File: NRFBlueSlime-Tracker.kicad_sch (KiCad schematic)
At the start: 70 parts, among them J1 GT-USB-7010ASV, SW1 TS-1088-AR02016, U1 nRF52840, U2 EA8103DHR, U3 BQ24075RGT, U4 ICM-45686, U5 LIS2MDL, X1 S2D32.768KB20F30T, Y1 XKXGI-SUA-32.768K, Y2 XL7EL89CKI-111YLC-32M

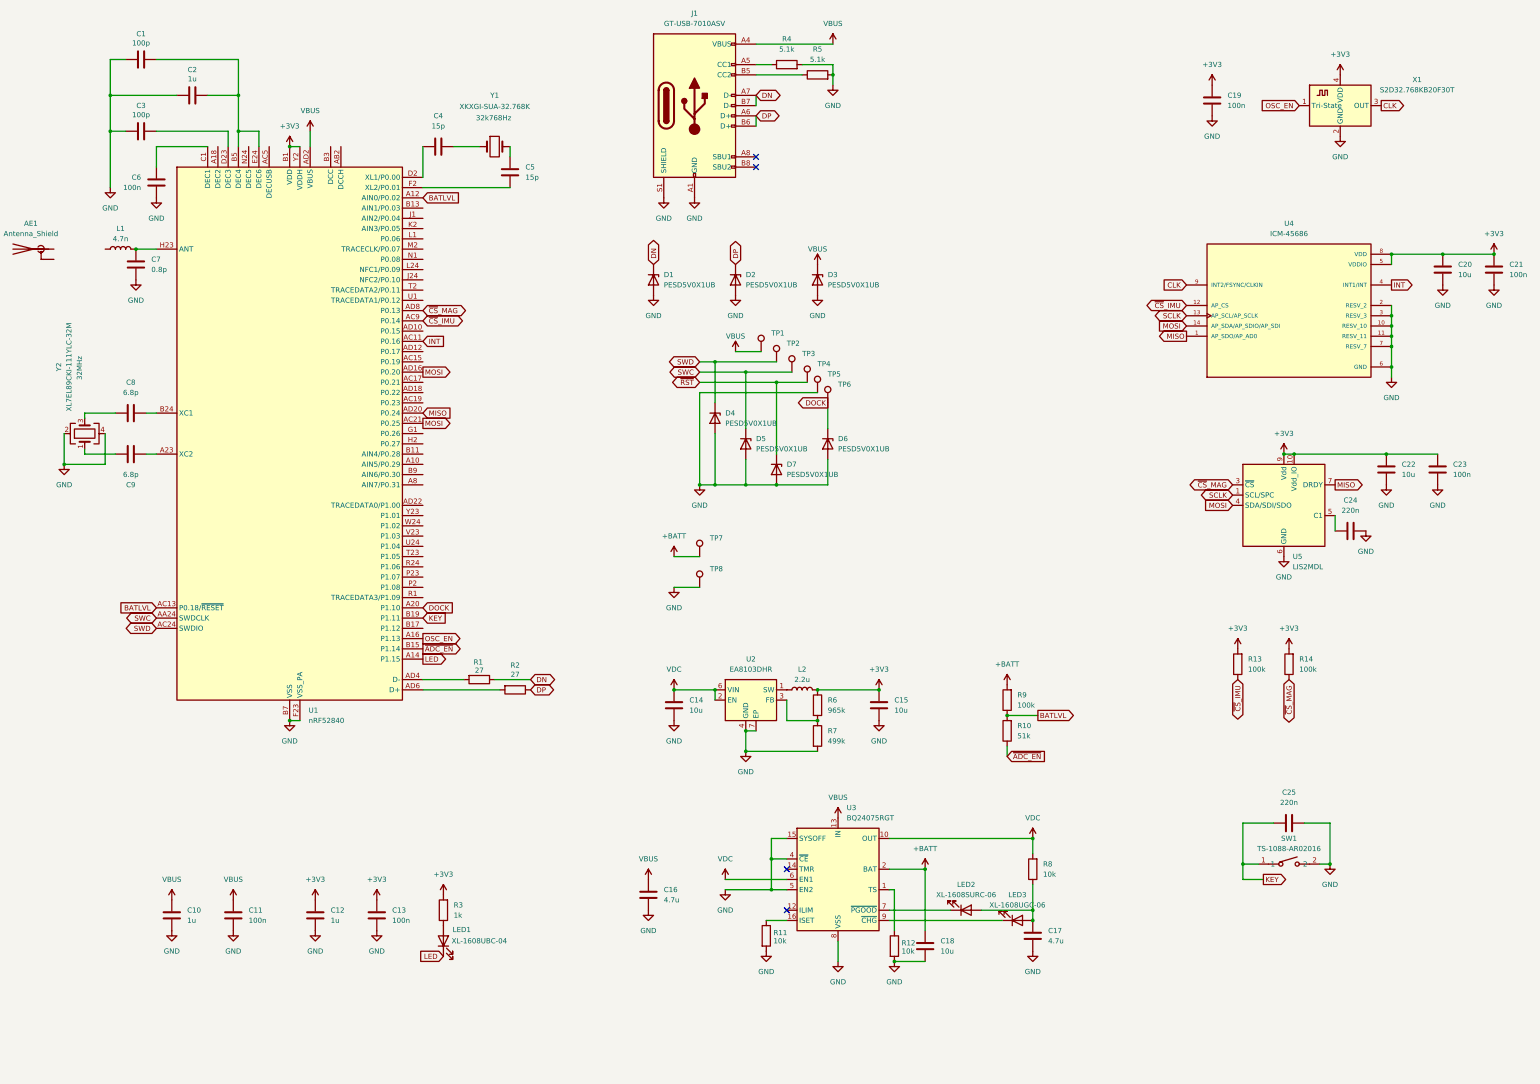
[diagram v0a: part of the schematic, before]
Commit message: rework LEDs
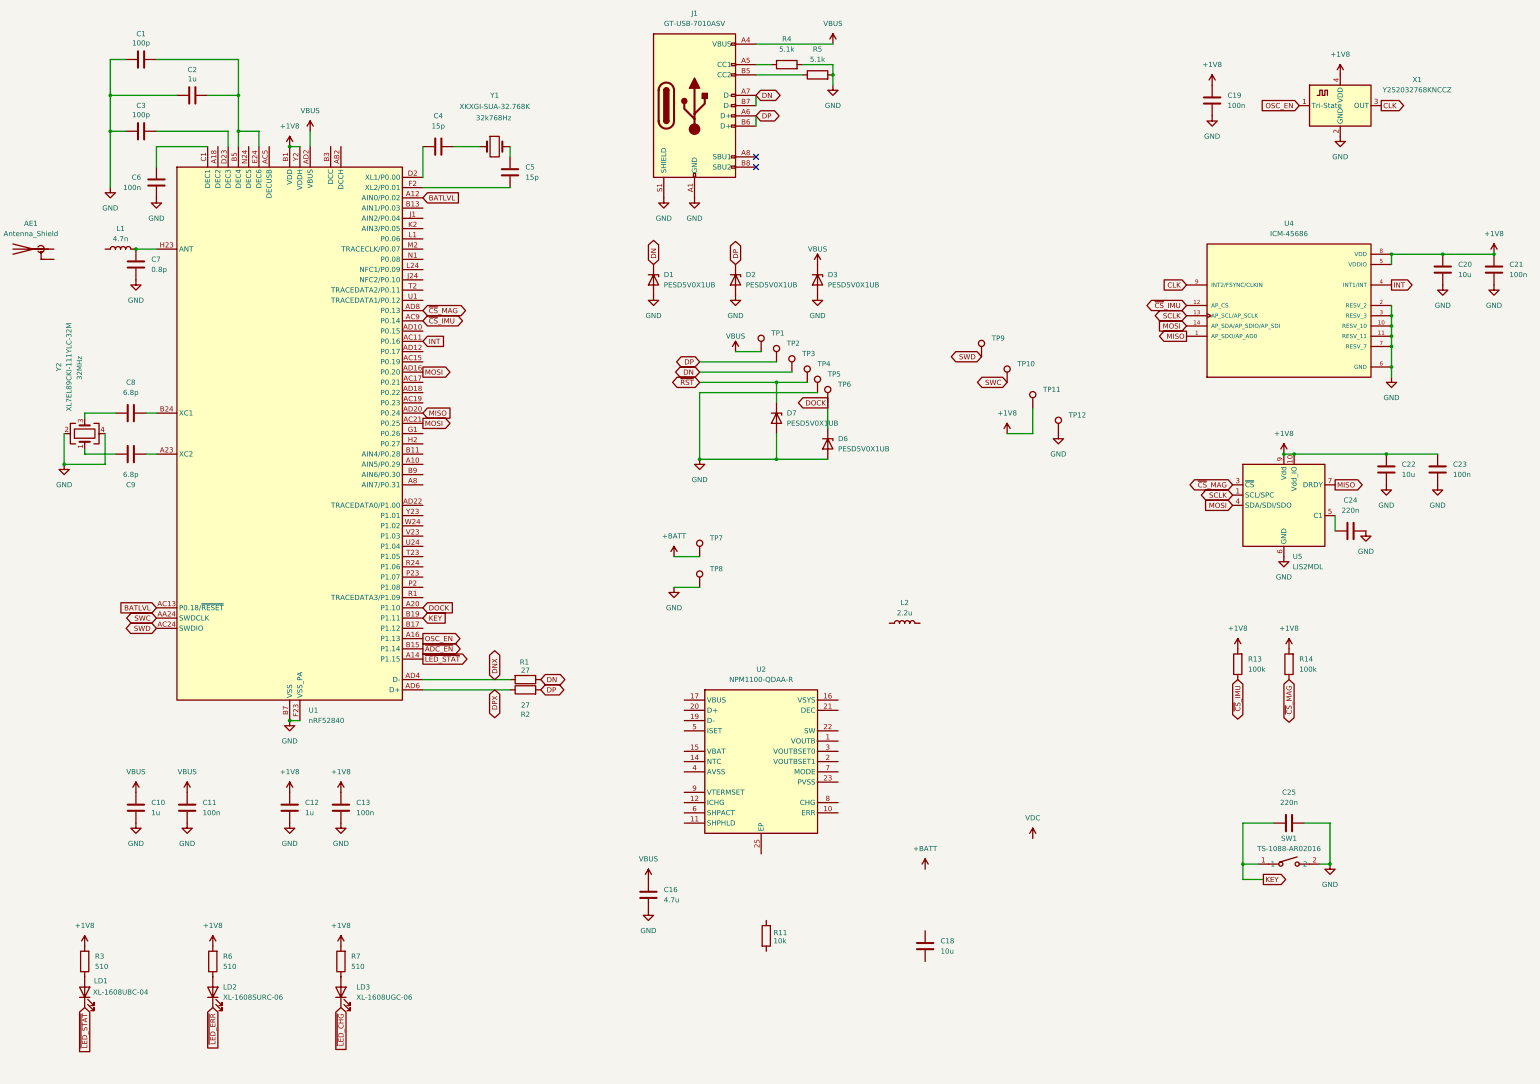
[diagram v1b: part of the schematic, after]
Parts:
- removed C14, C15: 10u, Capacitor_SMD:C_0603_1608Metric, symbol Device:C
- removed C17: 4.7u, Capacitor_SMD:C_0603_1608Metric, symbol Device:C
- removed D4, D5: PESD5V0X1UB, Diode_SMD:D_SOD-882, symbol Diode:PESD5V0L1UL
- removed R10: 51k, Resistor_SMD:R_0603_1608Metric, symbol Device:R
- removed R12, R8: 10k, Resistor_SMD:R_0402_1005Metric, symbol Device:R
- removed R9: 100k, Resistor_SMD:R_0603_1608Metric, symbol Device:R
- removed U2: EA8103DHR, nrfslime:DFN-6_L1.5-W1.5-P0.50-BL-EP1.0, symbol nrfslime:EA8103DHR
- removed U3: BQ24075RGT, Package_DFN_QFN:VQFN-16-1EP_3x3mm_P0.5mm_EP1.6x1.6mm, symbol Battery_Management:BQ24075RGT
- added TP10, TP11, TP12, TP9: TestPoint, TestPoint:TestPoint_Pad_1.0x1.0mm, symbol Connector:TestPoint
- added U2: NPM1100-QDAA-R, npm1100-q:QFN50P400X400X90-25N-D, symbol NPM1100-QDAA-R:NPM1100-QDAA-R
- R3: value 1k -> 510
- R6: value 965k -> 510
- R7: value 499k -> 510
- X1: value S2D32.768KB20F30T -> Y252032768KNCCZ
- renumbered LED1 to LD1, LED2 to LD2, LED3 to LD3
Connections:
- net +BATT: no longer C18.2
- net DN: now also TP3.1
- net DP: now also R2.2, TP2.1; no longer R2.1
- net GND: now also TP12.1; no longer C18.1, R11.2, R7.2
- net SWC: now also TP10.1; no longer TP3.1
- net SWD: now also TP9.1; no longer TP2.1
- net at LD3.2 (A): now also R7.1; no longer LD2.2 (A)
- net DNX: now reaches R1.2, U1.AD4 (D-)
- net +1V8: now reaches R6.2
- net +1V8: now also C12.1, C13.1, C19.1, C20.1, C21.1, C22.1, C23.1, R13.2, R14.2, R3.2, R7.2, U1.A22 (VDD), U1.AD14 (VDD), U1.AD23 (VDD), U1.B1 (VDD), U1.W1 (VDD), U1.Y2 (VDDH), U4.5 (VDDIO), U4.8 (VDD), U5.10 (Vdd_IO), U5.9 (Vdd), X1.4 (VDD), TP11.1; no longer R7.1
- net ~{LED_CHG}: now reaches LD3.1 (K)
- net ~{LED_ERR}: now reaches LD2.1 (K)
- net DPX: now reaches U1.AD6 (D+)
- net DPX: now also R2.1; no longer R2.2
- removed net +3V3: C12.1, C13.1, C19.1, C20.1, C21.1, C22.1, C23.1, L2.2, R13.2, R14.2, R3.2, R6.1, U1.A22 (VDD), U1.AD14 (VDD), U1.AD23 (VDD), U1.B1 (VDD), U1.W1 (VDD), U1.Y2 (VDDH), U4.5 (VDDIO), U4.8 (VDD), U5.10 (Vdd_IO), U5.9 (Vdd), X1.4 (VDD)
- net LED renamed ~{LED_STAT}
- new net: LD2.2 (A), R6.1
- no-connect marks 4 -> 2
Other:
- moved on the sheet: C10, C11, C12, C13, D7, L2, LD1, LD2, LD3, R1, R2, R3

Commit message: complete nPM
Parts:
- added C14, C15: 10u, Capacitor_SMD:C_0603_1608Metric, symbol Device:C
- added C17: 1u, Capacitor_SMD:C_0603_1608Metric, symbol Device:C
- added R10, R8, R9: 100k, Resistor_SMD:R_0402_1005Metric, symbol Device:R
- added TH1: HNTC0402-103F3380FB, Resistor_SMD:R_0402_1005Metric, symbol Device:Thermistor_NTC
- added TP13, TP14: TestPoint, TestPoint:TestPoint_Pad_1.0x1.0mm, symbol Connector:TestPoint
- C16: value 4.7u -> 2.2u
- R11: value 10k -> 4.7k
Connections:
- net +1V8: now also L2.2, U2.1 (VOUTB), C15.1
- net +BATT: now also U2.15 (VBAT), C17.2, R9.1
- net DN: now also R1.2, U1.AD4 (D-), U2.19 (D-); no longer J1.A7 (D-), J1.B7 (D-), R1.1
- net DNX: now also J1.A7 (D-), J1.B7 (D-), R1.1; no longer R1.2, U1.AD4 (D-)
- net DP: now also R2.1, U1.AD6 (D+), U2.20 (D+); no longer J1.A6 (D+), J1.B6 (D+), R2.2
- net DPX: now also J1.A6 (D+), J1.B6 (D+), R2.2; no longer R2.1, U1.AD6 (D+)
- net GND: now also C18.1, R11.2, U2.2 (VOUTBSET1), U2.23 (PVSS), U2.25 (EP), U2.4 (AVSS), C14.1, C15.2, C17.1, R10.1, R8.1, TH1.2
- net VBUS: now also U2.17 (VBUS)
- net ~{LED_CHG}: now also U1.L1 (P0.06)
- net ~{LED_ERR}: now also U1.N1 (P0.08)
- net at L2.1: now also U2.22 (SW)
- net VSYS: now reaches C18.2
- net VSYS: now also U2.16 (VSYS), U2.3 (VOUTBSET0), U2.9 (VTERMSET)
- net ISET: now reaches U1.R24 (P1.06)
- net ISET: now also U2.5 (ISET), R10.2
- net MODE: now reaches U1.T23 (P1.05)
- net MODE: now also U2.7 (MODE), R8.2
- net ~{NPM_ERR}: now reaches U1.U24 (P1.04)
- net ~{NPM_ERR}: now also U2.10 (ERR)
- net ~{NPM_CHG}: now reaches U1.V23 (P1.03)
- net ~{NPM_CHG}: now also U2.8 (CHG)
- net at R11.1: now also U2.12 (ICHG)
- net at U2.11 (SHPHLD): now also R9.2
- net NTC: now reaches U2.14 (NTC)
- net NTC: now also TH1.1, TP13.1
- net at U2.21 (DEC): now also C14.2
- net SHPACT: now reaches U2.6 (SHPACT)
- net SHPACT: now also TP14.1
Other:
- moved on the sheet: C16, C18, L2, R11, TP10, TP11, TP12, U2

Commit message: do usb dual mode
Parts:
- added C1: 4.7u, Capacitor_SMD:C_0603_1608Metric, symbol Device:C
- added L1: MGFL2012F150MT-LF, Inductor_SMD:L_0805_2012Metric, symbol Device:L
- added L2, L3: MLZ2012N100LT000, Inductor_SMD:L_0805_2012Metric, symbol Device:L
- added R1, R2: 0, Resistor_SMD:R_0603_1608Metric, symbol Device:R
- added R5: 1, Resistor_SMD:R_0603_1608Metric, symbol Device:R
- C11: renamed from C10; value 1u -> 4.7u
- C13: renamed from C12; value 1u -> 4.7u
- renumbered C9 to C10, C11 to C12, C13 to C14, C14 to C15, C18 to C16, C15 to C17, C16 to C18, C17 to C19, C1 to C2, C19 to C20, C20 to C21, C21 to C22, C22 to C23, C23 to C24, C24 to C25, C25 to C26, C2 to C3, C3 to C4, C4 to C5, C5 to C6, C6 to C7, C7 to C8, C8 to C9, D7 to D4, D6 to D5, L1 to L4, L2 to L5, R5 to R10, R9 to R11, R11 to R12, R8 to R13, R10 to R14, R13 to R15, R14 to R16, R1 to R3, R2 to R4, R3 to R6, R6 to R7, R7 to R8, R4 to R9, TP11 to TP10, TP12 to TP11, TP7 to TP12, TP8 to TP14, TP9 to TP7, TP14 to TP8, TP10 to TP9, U4 to U3, U5 to U4
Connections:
- net +1V8: now also L2.1, R1.2; no longer U1.Y2 (VDDH)
- net GND: now also C10.1, C9.1, C1.1
- net MOSI: no longer U1.AC21 (P0.25)
- net VBUS: now also R5.1; no longer C11.1, C12.1, U1.AD2 (VBUS)
- net ~{RST}: now also U1.AC13 (P0.18/~{RESET})
- net at Y2.3: now also C9.2, U1.B24 (XC1); no longer C9.1
- net at Y2.1: now also C10.2, U1.A23 (XC2); no longer C10.1
- net at C2.2, C3.2, U1.B5 (DEC4)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: now also L1.1
- net at U1.AB2 (DCCH): now also L2.2
- net at U1.AC5 (DECUSB): now also C1.2
- net at U1.B3 (DCC): now also L3.2
- net BATLVL: no longer names the net of U1.A12 (AIN0/P0.02)
- net BATLVL: no longer U1.AC13 (P0.18/~{RESET})
- net ISET renamed NPM_ISET
- net MODE renamed NPM_MODE
- net ~{NPM_CHG} renamed NPM_~{CHG}
- net ~{NPM_ERR} renamed NPM_~{ERR}
- new net: R1.1, R2.2, U1.Y2 (VDDH)
- new net: L1.2, L3.1
- new net VBUS_NRF: C11.1, C12.1, R2.1, R5.2, U1.AD2 (VBUS)
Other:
- moved on the sheet: AE1, C10, C11, C12, C13, C14, C2, C20, C21, C22, C23, C24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

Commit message: done sch
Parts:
- removed C5: 15p, Capacitor_SMD:C_0402_1005Metric, symbol Device:C
- removed L2, L3: MLZ2012N100LT000, Inductor_SMD:L_0805_2012Metric, symbol Device:L
- removed Y1: XKXGI-SUA-32.768K, Crystal:Crystal_SMD_3215-2Pin_3.2x1.5mm, symbol Device:Crystal
- added C14, C20: 1n, Capacitor_SMD:C_0402_1005Metric, symbol Device:C
- added Q1: YFW2301T, Package_TO_SOT_SMD:SOT-523, symbol Transistor_FET:Q_PMOS_GSD
- added R11: 1M, Resistor_SMD:R_0402_1005Metric, symbol Device:R
- added R16: 470k, Resistor_SMD:R_0402_1005Metric, symbol Device:R
- AE1: footprint (none) -> nrfslime:MIFA_BLE_ANT
- C6: value 15p -> 1.2p
- C7: renamed from C8; value 0.8p -> 1p
- L1: value MGFL2012F150MT-LF -> 2.2n; footprint Inductor_SMD:L_0805_2012Metric -> Inductor_SMD:L_0402_1005Metric; now fitted
- R14: renamed from R13; value 100k -> 470k
- R15: renamed from R14; value 100k -> 470k
- R17: renamed from R15; value 100k -> 470k
- R18: renamed from R16; value 100k -> 470k
- X1: value Y252032768KNCCZ -> SX2M32.768KM20F30TNN
- renumbered C11 to C10, C12 to C11, C13 to C12, C14 to C13, C20 to C21, C21 to C22, C22 to C23, C23 to C24, C24 to C25, C25 to C26, C26 to C27, C7 to C5, C9 to C8, C10 to C9, L4 to L2, L5 to L3, R11 to R12, R12 to R13, TP7 to TP1, TP5 to TP10, TP12 to TP11, TP13 to TP12, TP6 to TP13, TP8 to TP2, TP9 to TP3, TP10 to TP4, TP11 to TP5, TP1 to TP6, TP2 to TP7, TP3 to TP8, TP4 to TP9, Y2 to Y1
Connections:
- net +1V8: now also Q1.3 (D); no longer C21.1, X1.4 (VDD)
- net CLK: now also U1.D2 (XL1/P0.00)
- net GND: now also AE1.2 (Shield), C6.1, U1.F2 (XL2/P0.01), C14.2, C20.2, R11.2, R16.1; no longer J1.S1 (SHIELD)
- net at C2.2, C3.2, U1.B5 (DEC4)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: no longer L1.1
- net at AE1.1 (A): now also L1.1
- net at L1.2: now also C6.2, L2.1
- net OSC_EN: no longer names the net of X1.1 (Tri-State)
- net OSC_EN: now also C21.1, X1.4 (VDD), Q1.2 (S); no longer U1.A16 (P1.13)
- new net: C14.1, J1.S1 (SHIELD), R11.1
- new net ~{OSC_EN}: C20.1, Q1.1 (G), R16.2, U1.A16 (P1.13)
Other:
- moved on the sheet: AE1, C15, C16, C17, C18, C19, C21, C22, C23, C24, C25, C26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

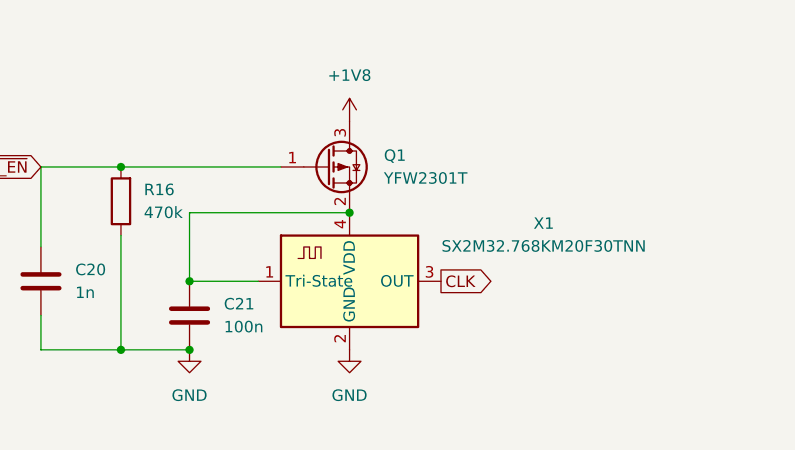
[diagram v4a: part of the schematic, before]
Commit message: fix mosfet upside down
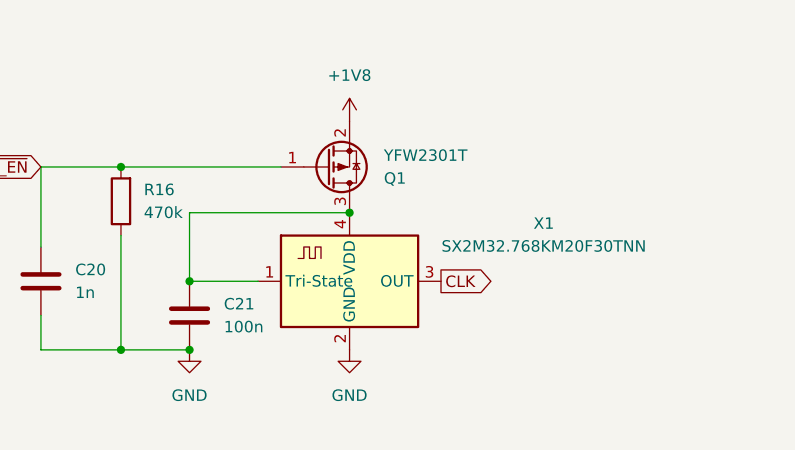
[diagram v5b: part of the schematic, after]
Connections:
- net +1V8: now also Q1.2 (S); no longer Q1.3 (D)
- net at C21.1, X1.1 (Tri-State), X1.4 (VDD): now also Q1.3 (D); no longer Q1.2 (S)
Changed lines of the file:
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@@
 	)
 	(junction
+		(at 355.6 44.45)
+		(diameter 0)
+		(color 0 0 0 0)
+	)
+	(junction
 		(at 44.45 53.34)
 		(diameter 0)
@@
 	)
 	(junction
-		(at 355.6 44.45)
-		(diameter 0)
-		(color 0 0 0 0)
-	)
-	(junction
 		(at 266.7 203.2)
 		(diameter 0)
@@
 		(lib_id "Transistor_FET:Q_PMOS_GSD")
 		(at 353.06 39.37 0)
+		(mirror x)
 		(unit 1)
 		(exclude_from_sim no)
@@
 		(on_board yes)
 		(dnp no)
-		(fields_autoplaced yes)
 		(property "Reference" "Q1"
-			(at 359.41 38.0999 0)
+			(at 359.41 40.6401 0)
 			(effects
 				(font
@@
 		)
 		(property "Value" "YFW2301T"
-			(at 359.41 40.6399 0)
+			(at 359.41 38.1001 0)
 			(effects
 				(font
@@
 		)
 		(property "Footprint" "Package_TO_SOT_SMD:SOT-523"
-			(at 358.14 36.83 0)
+			(at 358.14 41.91 0)
 			(effects
 				(font

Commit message: place components
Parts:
- C14: value 1n -> 100n
- J1: value GT-USB-7010ASV -> HC-TYPE-C-16P-C10B; footprint Connector_USB:USB_C_Receptacle_G-Switch_GT-USB-7010ASV -> nrfslime:USB-C-SMD_HC-TYPE-C-16P-C10B
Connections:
- net DN: no longer D1.1 (K)
- net DNX: now also D1.1 (K)
- net DP: no longer D2.1 (K)
- net DPX: now also D2.1 (K)
- net INT: now also U1.AD10 (P0.15); no longer U1.AC11 (P0.16)
- net NPM_MODE: now also U1.P23 (P1.07); no longer U1.T23 (P1.05)
- net NPM_~{CHG}: now also U1.W24 (P1.02); no longer U1.V23 (P1.03)
- net SCLK: now also U1.AC21 (P0.25)
- net ~{ADC_EN}: now also U1.A8 (AIN7/P0.31); no longer U1.B15 (P1.14)
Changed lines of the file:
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@@
 		)
 	)
-	(global_label "~{ADC_EN}"
-		(shape output)
-		(at 121.92 181.61 0)
-		(fields_autoplaced yes)
-		(effects
-			(font
-				(size 1.27 1.27)
-			)
-			(justify left)
-		)
-		(property "Intersheetrefs" "${INTERSHEET_REFS}"
-			(at 131.9809 181.61 0)
-			(effects
-				(font
-					(size 1.524 1.524)
-				)
-				(justify left)
-				(hide yes)
-			)
-		)
-	)
 	(global_label "MOSI"
 		(shape output)
@@
 		)
 	)
-	(global_label "NPM_~{CHG}"
-		(shape input)
-		(at 121.92 153.67 0)
-		(fields_autoplaced yes)
-		(effects
-			(font
-				(size 1.27 1.27)
-			)
-			(justify left)
-		)
-		(property "Intersheetrefs" "${INTERSHEET_REFS}"
-			(at 133.7952 153.67 0)
-			(effects
-				(font
-					(size 1.27 1.27)
-				)
-				(justify left)
-				(hide yes)
-			)
-		)
-	)
 	(global_label "~{LED_CHG}"
 		(shape input)
@@
 		)
 	)
+	(global_label "NPM_~{CHG}"
+		(shape input)
+		(at 121.92 151.13 0)
+		(fields_autoplaced yes)
+		(effects
+			(font
+				(size 1.27 1.27)
+			)
+			(justify left)
+		)
+		(property "Intersheetrefs" "${INTERSHEET_REFS}"
+			(at 133.7952 151.13 0)
+			(effects
+				(font
+					(size 1.27 1.27)
+				)
+				(justify left)
+				(hide yes)
+			)
+		)
+	)
 	(global_label "NPM_ISET"
-		(shape bidirectional)
+		(shape output)
 		(at 121.92 161.29 0)
 		(fields_autoplaced yes)
@@
 		)
 		(property "Intersheetrefs" "${INTERSHEET_REFS}"
-			(at 134.9669 161.29 0)
+			(at 133.8556 161.29 0)
 			(effects
 				(font
@@
 		)
 	)
-	(global_label "DP"
+	(global_label "DPX"
 		(shape bidirectional)
 		(at 213.36 124.46 90)
@@
 		)
 		(property "Intersheetrefs" "${INTERSHEET_REFS}"
-			(at 213.36 117.8235 90)
+			(at 213.36 116.614 90)
 			(effects
 				(font
@@
 		)
 	)
+	(global_label "~{ADC_EN}"
+		(shape output)
+		(at 121.92 140.97 0)
+		(fields_autoplaced yes)
+		(effects
+			(font
+				(size 1.27 1.27)
+			)
+			(justify left)
+		)
+		(property "Intersheetrefs" "${INTERSHEET_REFS}"
+			(at 131.9809 140.97 0)
+			(effects
+				(font
+					(size 1.524 1.524)
+				)
+				(justify left)
+				(hide yes)
+			)
+		)
+	)
 	(global_label "NTC"
 		(shape input)
@@
 		)
 	)
+	(global_label "INT"
+		(shape input)
+		(at 121.92 102.87 0)
+		(fields_autoplaced yes)
+		(effects
+			(font
+				(size 1.27 1.27)
+			)
+			(justify left)
+		)
+		(property "Intersheetrefs" "${INTERSHEET_REFS}"
+			(at 127.236 102.9494 0)
+			(effects
+				(font
+					(size 1.27 1.27)
+				)
+				(justify left)
+				(hide yes)
+			)
+		)
+	)
 	(global_label "~{LED_ERR}"
 		(shape input)
@@
 		)
 	)
+	(global_label "SCLK"
+		(shape bidirectional)
+		(at 121.92 125.73 0)
+		(fields_autoplaced yes)
+		(effects
+			(font
+				(size 1.27 1.27)
+			)
+			(justify left)
+		)
+		(property "Intersheetrefs" "${INTERSHEET_REFS}"
+			(at 130.7941 125.73 0)
+			(effects
+				(font
+					(size 1.27 1.27)
+				)
+				(justify left)
+				(hide yes)
+			)
+		)
+	)
 	(global_label "DN"
 		(shape bidirectional)
@@
 		)
 	)
-	(global_label "NPM_MODE"
-		(shape bidirectional)
-		(at 121.92 158.75 0)
-		(fields_autoplaced yes)
-		(effects
-			(font
-				(size 1.27 1.27)
-			)
-			(justify left)
-		)
-		(property "Intersheetrefs" "${INTERSHEET_REFS}"
-			(at 136.2369 158.75 0)
-			(effects
-				(font
-					(size 1.27 1.27)
-				)
-				(justify left)
-				(hide yes)
-			)
-		)
-	)
 	(global_label "~{RST}"
 		(shape bidirectional)
@@
 		)
 	)
-	(global_label "DN"
+	(global_label "DNX"
 		(shape bidirectional)
 		(at 193.04 124.46 90)
@@
 		)
 		(property "Intersheetrefs" "${INTERSHEET_REFS}"
-			(at 193.04 117.763 90)
+			(at 193.04 116.5535 90)
 			(effects
 				(font
@@
 		)
 	)
-	(global_label "INT"
+	(global_label "CLK"
 		(shape input)
-		(at 121.92 105.41 0)
+		(at 317.5 96.52 180)
 		(fields_autoplaced yes)
 		(effects
@@
 				(size 1.27 1.27)
 			)
-			(justify left)
+			(justify right)
 		)
 		(property "Intersheetrefs" "${INTERSHEET_REFS}"
-			(at 127.236 105.4894 0)
+			(at 310.9467 96.52 0)
 			(effects
 				(font
 					(size 1.27 1.27)
 				)
-				(justify left)
+				(justify right)
 				(hide yes)
 			)
 		)
 	)
-	(global_label "CLK"
-		(shape input)
-		(at 317.5 96.52 180)
+	(global_label "DNX"
+		(shape bidirectional)
+		(at 151.13 189.23 0)
 		(fields_autoplaced yes)
 		(effects
@@
 				(size 1.27 1.27)
 			)
-			(justify right)
+			(justify left)
 		)
 		(property "Intersheetrefs" "${INTERSHEET_REFS}"
-			(at 310.9467 96.52 0)
+			(at 159.0365 189.23 0)
 			(effects
 				(font
 					(size 1.27 1.27)
 				)
-				(justify right)
+				(justify left)
 				(hide yes)
 			)
 		)
 	)
-	(global_label "DNX"
-		(shape bidirectional)
-		(at 151.13 189.23 0)
+	(global_label "NPM_MODE"
+		(shape output)
+		(at 121.92 163.83 0)
 		(fields_autoplaced yes)
 		(effects
@@
 		)
 		(property "Intersheetrefs" "${INTERSHEET_REFS}"
-			(at 159.0365 189.23 0)
+			(at 135.1256 163.83 0)
 			(effects
 				(font
@@
 			)
 		)
-		(property "Value" "1n"
+		(property "Value" "100n"
 			(at 205.74 88.9 90)
 			(effects
@@
 			)
 		)
-		(property "Value" "GT-USB-7010ASV"
+		(property "Value" "HC-TYPE-C-16P-C10B"
 			(at 209.55 45.72 0)
 			(effects
@@
 			)
 		)
-		(property "Footprint" "Connector_USB:USB_C_Receptacle_G-Switch_GT-USB-7010ASV"
+		(property "Footprint" "nrfslime:USB-C-SMD_HC-TYPE-C-16P-C10B"
 			(at 213.36 66.04 0)
 			(effects
